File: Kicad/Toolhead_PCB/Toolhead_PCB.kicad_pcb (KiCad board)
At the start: 2 copper layers, 49.8 x 29 mm, 19 parts, among them J1 Conn_02x10_Top_Bottom, J2 Motor, J3 Hotend Fan, J4 Part Cooling Fan, J5 Heater, J6 Thermistor, J7 X-Endstop, J8 Part Cooling Fan, U1 ADXL345BCCZ, U2 LP2985-33DBVR

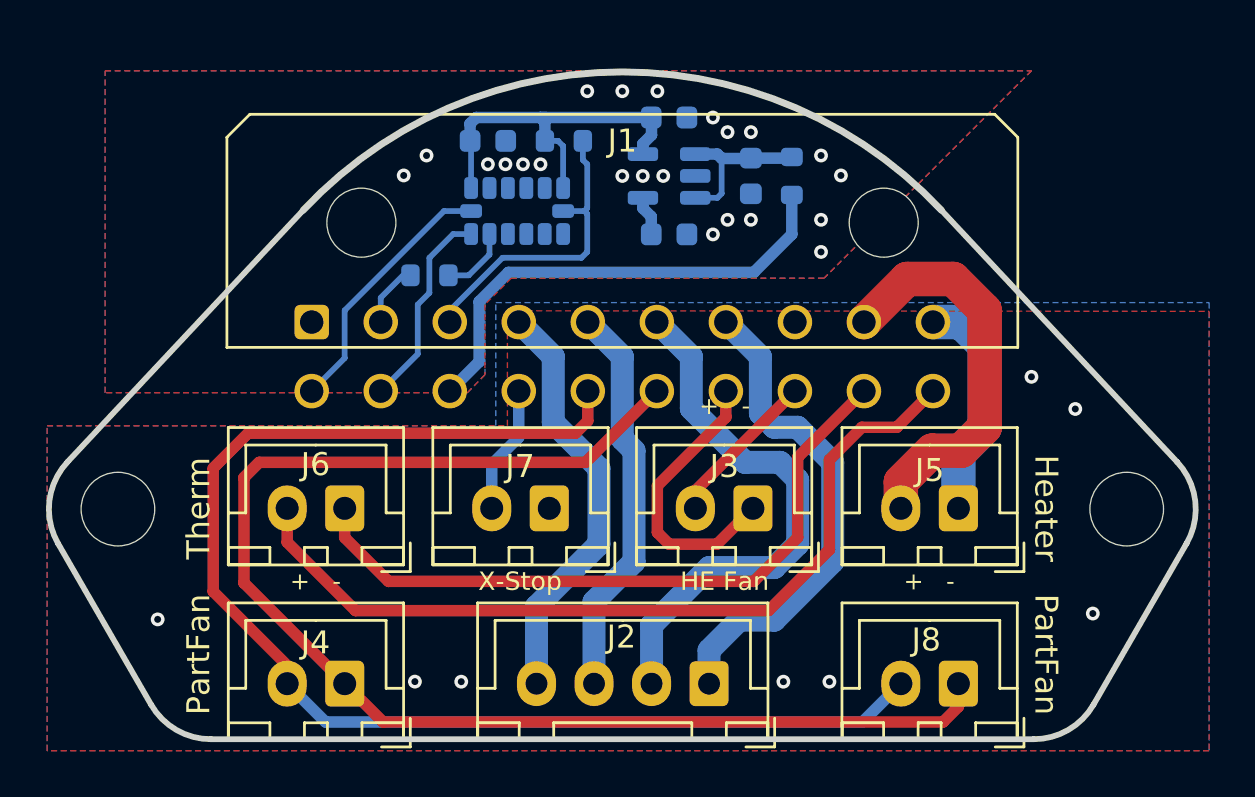
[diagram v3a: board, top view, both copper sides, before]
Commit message: Switch LDO to more available part. Migrate to JLCPBC Kicad plugin for maintainability
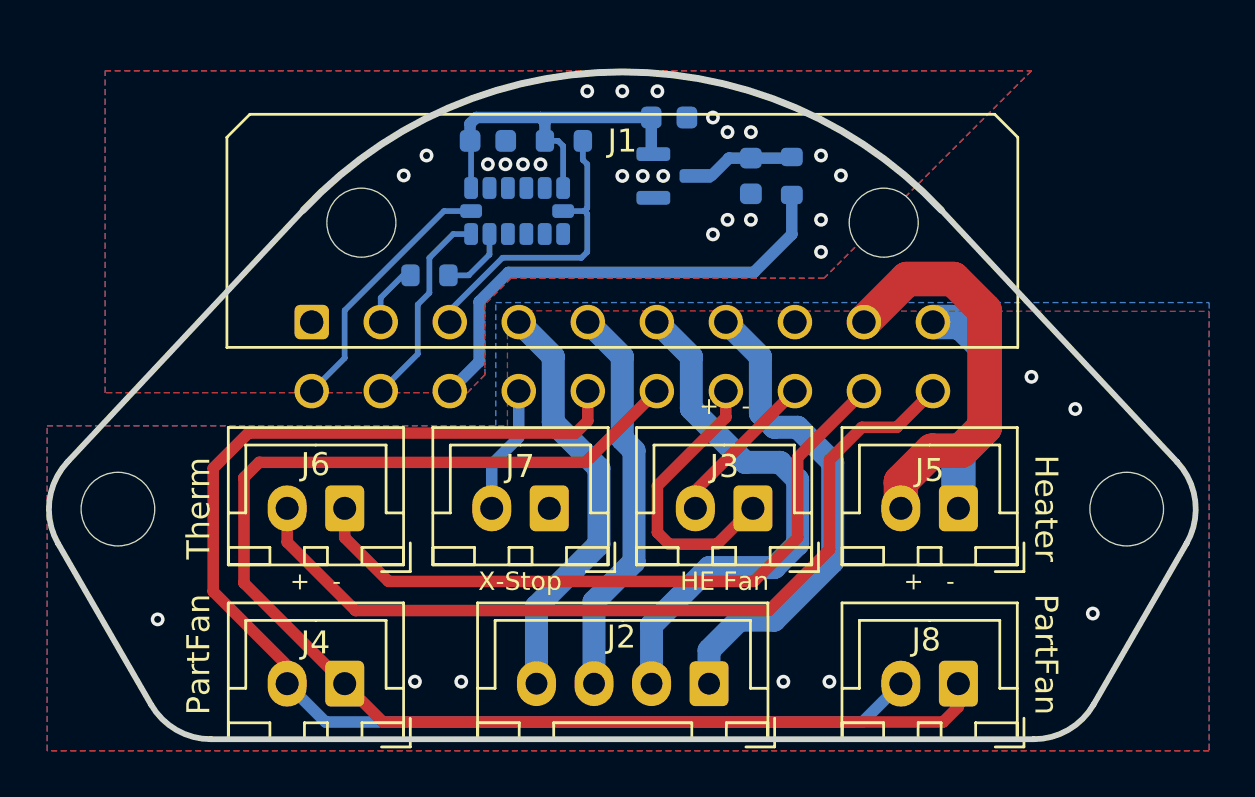
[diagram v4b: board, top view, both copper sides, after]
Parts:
- removed C2: 10n/NP0, Capacitor_SMD:C_0603_1608Metric
- U2: value LP2985-33DBVR -> XC6206PxxxMR; footprint Package_TO_SOT_SMD:SOT-23-5 -> Package_TO_SOT_SMD:SOT-23
- moved U2 0.25 mm to (102.3, 85.5), turned to 0 degrees
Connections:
- U2 pad 1: Net-(C1-Pad1) -> GND1
- U2 pad 2: GND1 -> +3V3
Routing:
- net Net-(C1-Pad1): track 7.05 -> 3.78 mm
- net Net-(C2-Pad1): track 1.74 -> 0.00 mm
- net +3V3: track 16.6 -> 16.0 mm
- net /ADXL_CS: track 13.5 -> 13.0 mm
